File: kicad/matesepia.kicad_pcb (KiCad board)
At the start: 2 copper layers, 225.3 x 129.3 mm, 63 parts

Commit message: syncing to desktop app
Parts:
- moved D22 5.20 mm to (197.5, 107.0)
- moved S22 5.20 mm to (194.8, 102.8)
- moved S28 5.20 mm to (110.4, 154.1)
- moved S30 5.20 mm to (183.2, 154.1)
- moved S1 5.20 mm to (44.1, 84.8)
- moved S26 5.20 mm to (164.3, 90.2)
- moved D11 5.20 mm to (116.4, 74.9)
- moved D12 5.20 mm to (116.3, 110.5)
- moved D13 5.20 mm to (126.5, 94.4)
- moved D15 5.20 mm to (244.0, 71.9)
- moved D2 5.20 mm to (49.5, 71.9)
- moved D20 5.20 mm to (198.7, 73.5)
- moved D24 5.20 mm to (177.1, 74.9)
- moved D25 5.20 mm to (177.2, 110.5)
- moved D26 5.20 mm to (167.0, 94.4)
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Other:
- board size 225.3 x 129.3 mm -> 227.7 x 131.8 mm

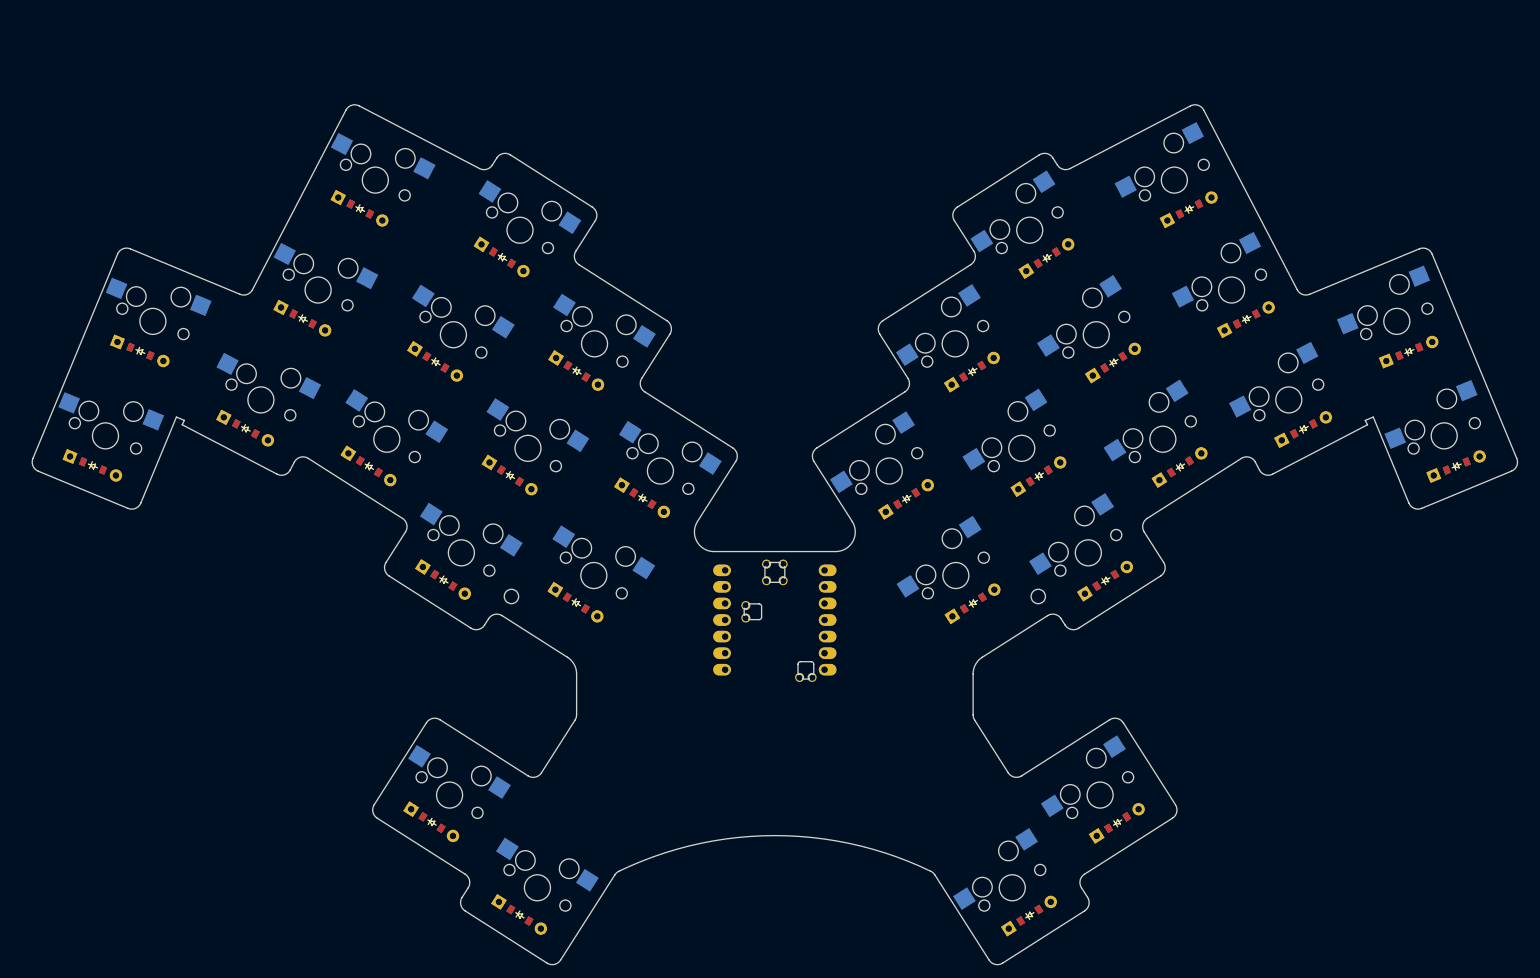
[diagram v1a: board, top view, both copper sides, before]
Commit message: correct matesepia to metasepia everywhere
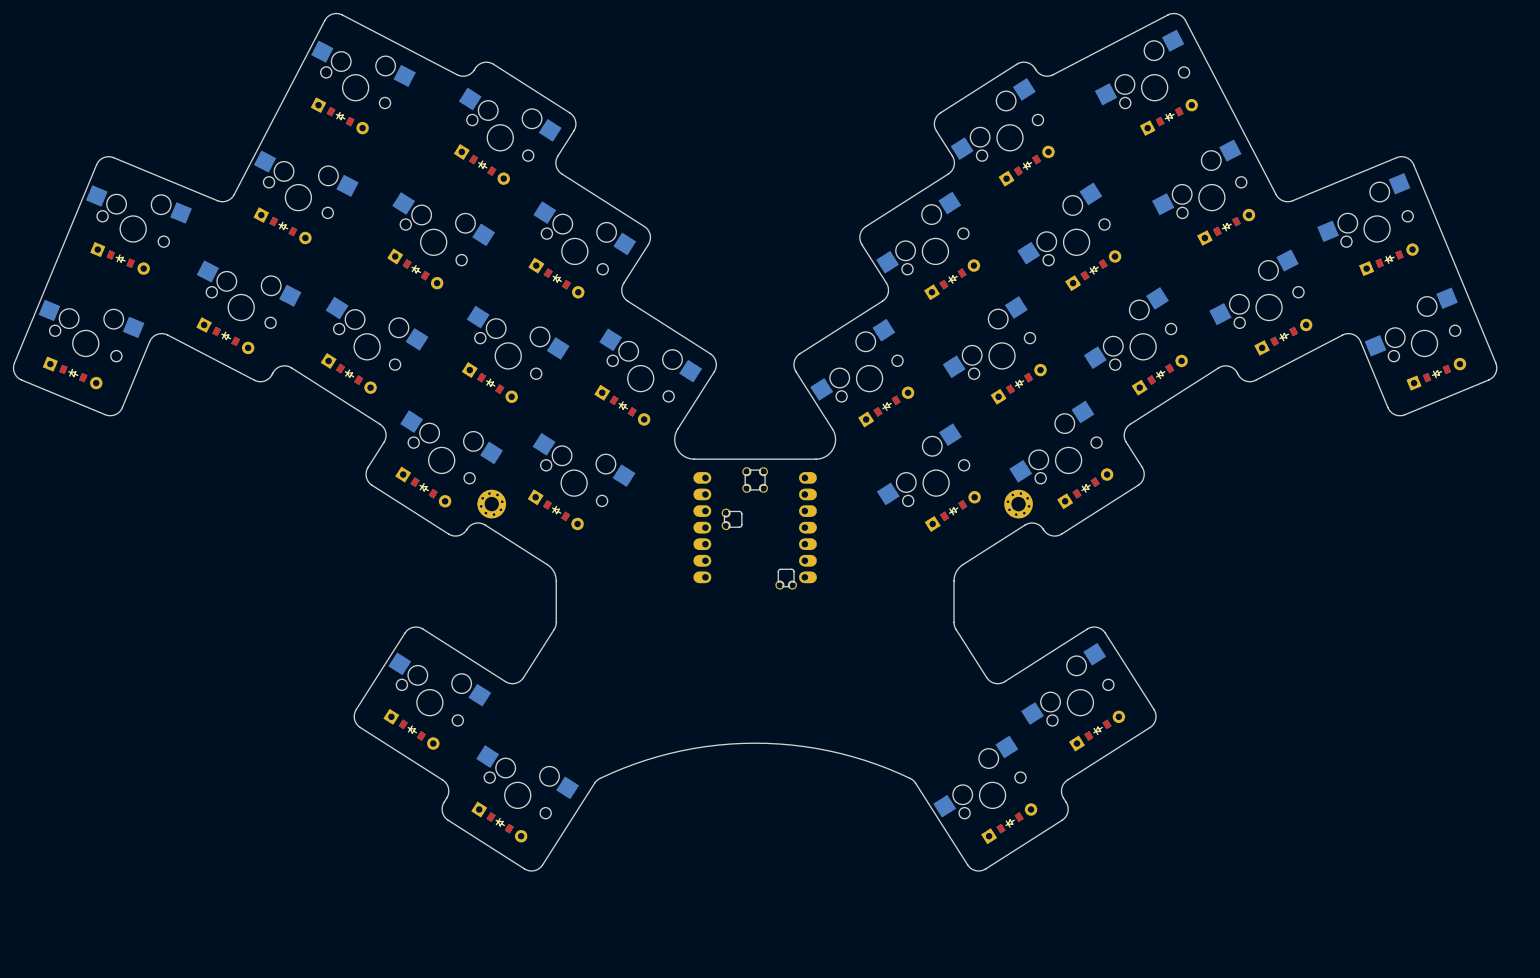
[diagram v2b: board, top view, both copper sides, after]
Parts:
- removed MH1, MH2: , ceoloide:mounting_hole_npth
- added _1: , MountingHole_2.2mm_M2_Pad_Via, F.Cu at (103.3, 95.3)
- added _2: , MountingHole_2.2mm_M2_Pad_Via, F.Cu at (184.1, 95.3)
- moved D10 14.5 mm to (103.2, 76.8)
- moved D11 14.5 mm to (113.4, 60.8)
- moved D13 14.5 mm to (123.5, 80.3)
- moved D2 14.5 mm to (46.5, 57.7)
- moved D23 14.5 mm to (184.3, 76.8)
- moved D24 14.5 mm to (174.1, 60.8)
- moved D25 14.5 mm to (174.2, 96.3)
- moved D27 14.5 mm to (91.2, 130.0)
- moved D29 14.5 mm to (196.3, 130.0)
- moved D30 14.5 mm to (182.8, 144.2)
- moved D7 14.5 mm to (91.8, 59.4)
- moved D9 14.5 mm to (93.0, 92.8)
- moved MCU1 14.5 mm to (143.7, 98.9)
- moved S1 14.5 mm to (41.1, 70.7)
- moved S10 14.5 mm to (105.9, 72.6)
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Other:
- board size 227.7 x 131.8 mm -> 227.4 x 131.5 mm
